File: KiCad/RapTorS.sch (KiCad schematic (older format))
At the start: 28 parts, among them IC1 EFM32HG308F64G-A-QFN24, J1 Molex 48037-2200, J2 TestPoint, J3 TestPoint, J4 TestPoint, J5 TestPoint, J6 TestPoint, SW1 SW_Push, U2 TLV71333PDBV, U3 E07-M1101S

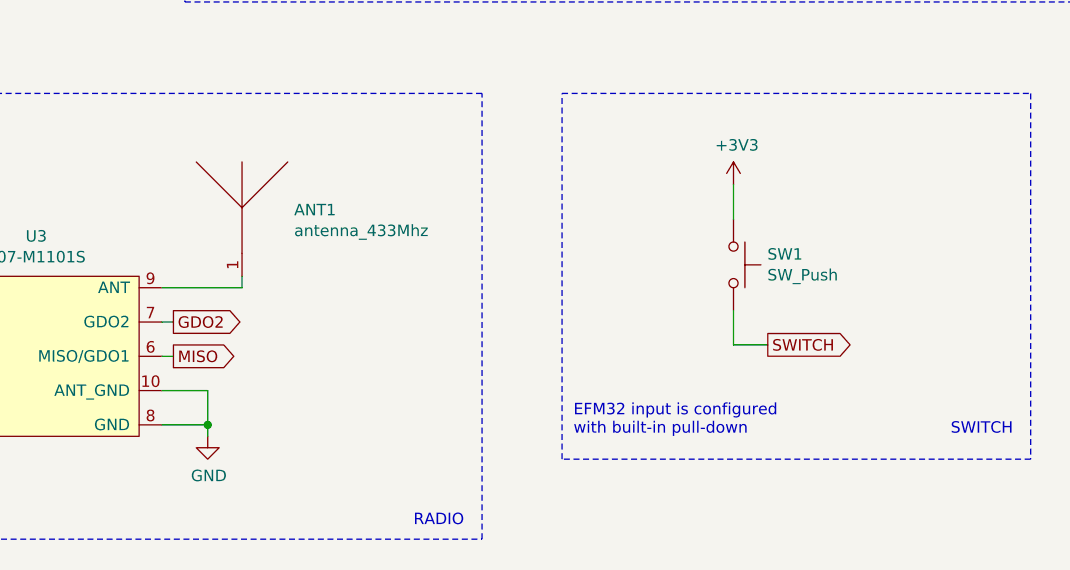
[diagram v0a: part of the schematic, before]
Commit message: change wire antenna by SMA connector
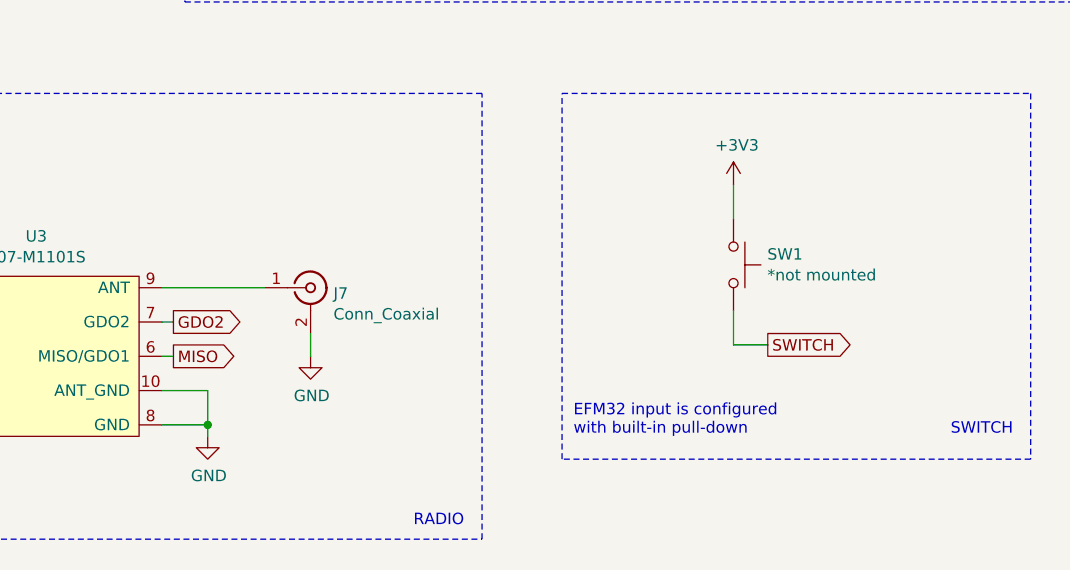
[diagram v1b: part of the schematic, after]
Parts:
- removed ANT1: antenna_433Mhz, Connectors:Pin_d1.0mm_L10.0mm, symbol RapTorS-rescue:antenna_433Mhz-antenna
- added J7: Conn_Coaxial, symbol Connector:Conn_Coaxial
- SW1: value SW_Push -> *not mounted
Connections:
- net GND: now also J7.2 (Ext)
- net at U3.9 (ANT): now also J7.1 (In)
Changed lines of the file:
@@
 $EndDescr
-$Comp
-L RapTorS-rescue:antenna_433Mhz-antenna ANT1
-U 1 1 5B61E0D6
-P 5650 4850
-F 0 "ANT1" H 5878 4540 50  0000 L CNN
-F 1 "antenna_433Mhz" H 5878 4449 50  0000 L CNN
-F 2 "Connectors:Pin_d1.0mm_L10.0mm" H 5650 4850 50  0001 C CNN
-F 3 "" H 5650 4850 50  0001 C CNN
-	1    5650 4850
-	1    0    0    -1
-$EndComp
 $Comp
 L Connector:USB_A J1
@@
 	1    0    0    -1
 $EndComp
-Wire Wire Line
-	5300 5500 5650 5500
-Wire Wire Line
-	5650 5500 5650 5450
 $Comp
 L power:GND #PWR020
@@
 P 7800 5400
 F 0 "SW1" V 7754 5548 50  0000 L CNN
-F 1 "SW_Push" V 7845 5548 50  0000 L CNN
+F 1 "*not mounted" V 7845 5548 50  0000 L CNN
 F 2 "" H 7800 5600 50  0001 C CNN
 F 3 "~" H 7800 5600 50  0001 C CNN
@@
 Text Notes 7100 6150 0    50   ~ 0
 EFM32 input is configured\nwith built-in pull-down
+$Comp
+L Connector:Conn_Coaxial J7
+U 1 1 5DA1EEE0
+P 5950 5500
+F 0 "J7" H 6050 5475 50  0000 L CNN
+F 1 "Conn_Coaxial" H 6050 5384 50  0000 L CNN
+F 2 "" H 5950 5500 50  0001 C CNN
+F 3 " ~" H 5950 5500 50  0001 C CNN
+	1    5950 5500
+	1    0    0    -1
+$EndComp
+$Comp
+L power:GND #PWR021
+U 1 1 5DA2324C
+P 5950 5800
+F 0 "#PWR021" H 5950 5550 50  0001 C CNN
+F 1 "GND" H 5955 5627 50  0000 C CNN
+F 2 "" H 5950 5800 50  0001 C CNN
+F 3 "" H 5950 5800 50  0001 C CNN
+	1    5950 5800
+	1    0    0    -1
+$EndComp
+Wire Wire Line
+	5950 5700 5950 5800
+Wire Wire Line
+	5300 5500 5750 5500
 $EndSCHEMATC
